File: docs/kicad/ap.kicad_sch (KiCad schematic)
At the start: 5 parts, among them U5 ESP32-DevKitC

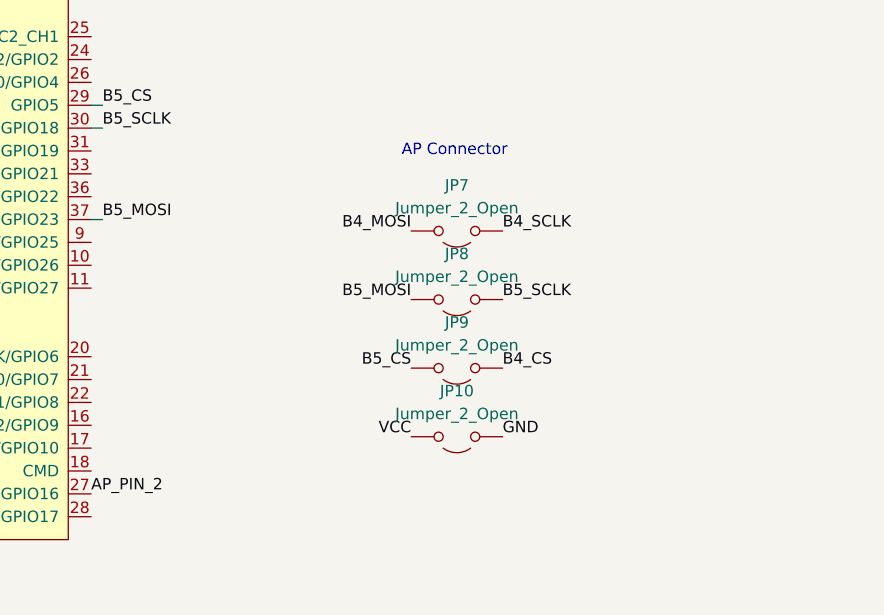
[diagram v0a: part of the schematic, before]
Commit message: Shrink PCB + minor modifications
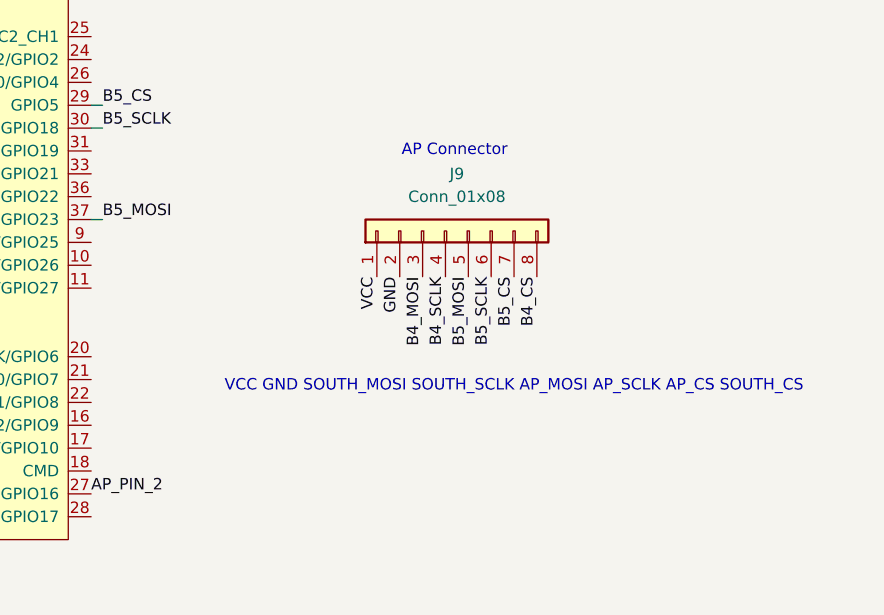
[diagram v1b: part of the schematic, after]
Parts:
- removed JP10, JP7, JP8, JP9: Jumper_2_Open, Connector_PinSocket_1.00mm:PinSocket_1x02_P1.00mm_Vertical, symbol Jumper:Jumper_2_Open
- added J9: Conn_01x08, Connector_PinHeader_1.27mm:PinHeader_1x08_P1.27mm_Vertical, symbol Connector_Generic:Conn_01x08
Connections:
- net B4_CS: now also J9.8 (Pin_8)
- net B4_MOSI: now also J9.3 (Pin_3)
- net B4_SCLK: now also J9.4 (Pin_4)
- net B5_CS: now also J9.7 (Pin_7)
- net B5_MOSI: now also J9.5 (Pin_5)
- net B5_SCLK: now also J9.6 (Pin_6)
- net GND1: now also J9.2 (Pin_2)
- net VCC: now also J9.1 (Pin_1)
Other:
- note added: "VCC GND SOUTH_MOSI SOUTH_SCLK AP_MOSI AP_SCLK AP_CS SOUTH_CS"

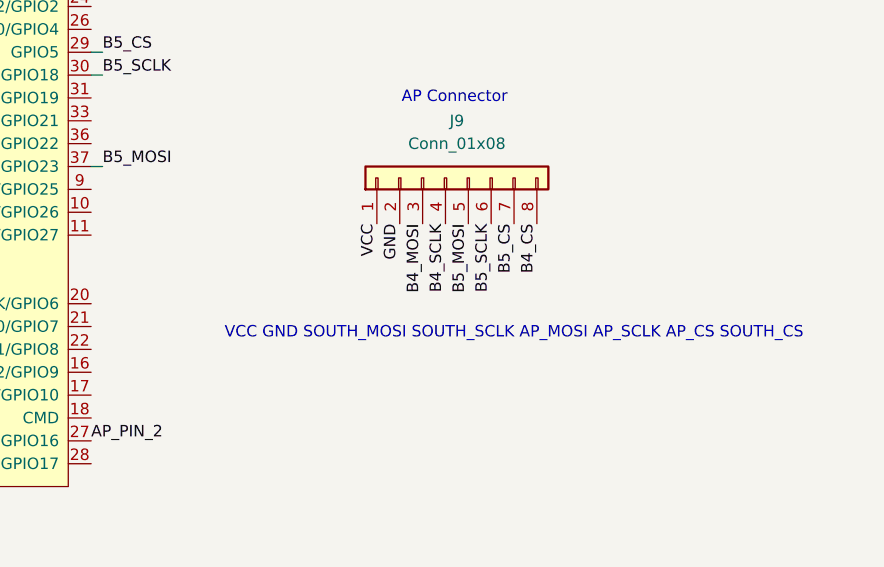
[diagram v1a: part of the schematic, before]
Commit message: used 8mm routes 1mm clearance, having some gnd islands
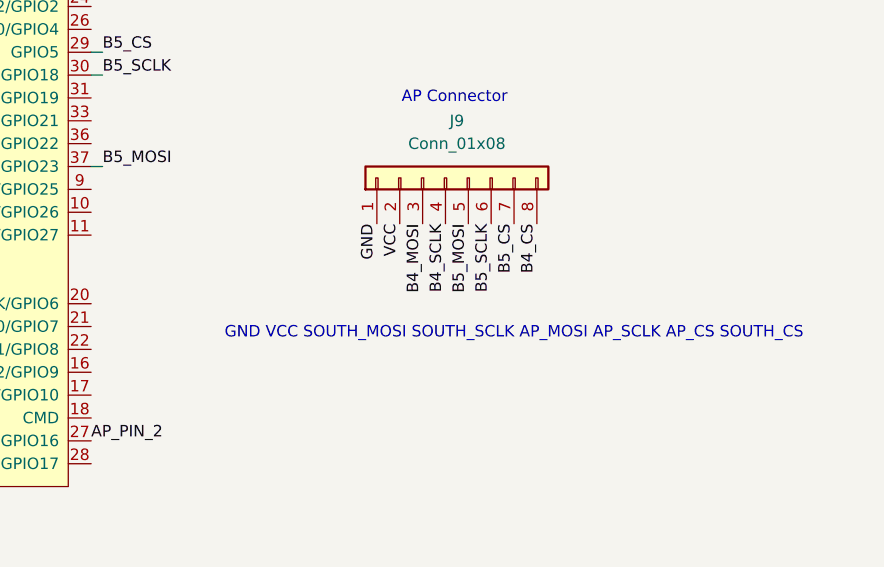
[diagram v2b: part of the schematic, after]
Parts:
- J9: footprint Connector_PinHeader_1.27mm:PinHeader_1x08_P1.27mm_Vertical -> Connector_PinSocket_2.54mm:PinSocket_1x08_P2.54mm_Vertical
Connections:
- net GND1: now also J9.1 (Pin_1); no longer J9.2 (Pin_2)
- net VCC: now also J9.2 (Pin_2); no longer J9.1 (Pin_1)
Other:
- note added: "GND VCC SOUTH_MOSI SOUTH_SCLK AP_MOSI AP_SCLK AP_CS SOUTH_CS"
- note removed: "VCC GND SOUTH_MOSI SOUTH_SCLK AP_MOSI AP_SCLK AP_CS SOUTH_CS"
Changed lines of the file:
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@@
 		)
 	)
-	(text "VCC GND SOUTH_MOSI SOUTH_SCLK AP_MOSI AP_SCLK AP_CS SOUTH_CS"
+	(text "GND VCC SOUTH_MOSI SOUTH_SCLK AP_MOSI AP_SCLK AP_CS SOUTH_CS"
 		(exclude_from_sim no)
 		(at 137.16 80.772 0)
@@
 		)
 	)
-	(label "GND"
-		(at 124.46 68.58 270)
-		(fields_autoplaced yes)
-		(effects
-			(font
-				(size 1.27 1.27)
-			)
-			(justify right bottom)
-		)
-	)
 	(label "B4_SCLK"
 		(at 129.54 68.58 270)
@@
 		)
 	)
+	(label "VCC"
+		(at 124.46 68.58 270)
+		(fields_autoplaced yes)
+		(effects
+			(font
+				(size 1.27 1.27)
+			)
+			(justify right bottom)
+		)
+	)
 	(label "B5_SCLK"
 		(at 134.62 68.58 270)
@@
 		)
 	)
-	(label "VCC"
-		(at 121.92 68.58 270)
-		(fields_autoplaced yes)
-		(effects
-			(font
-				(size 1.27 1.27)
-			)
-			(justify right bottom)
-		)
-	)
 	(label "GND"
 		(at 57.15 100.33 270)
@@
 	(label "B4_SCLK"
 		(at 22.86 52.07 180)
+		(fields_autoplaced yes)
+		(effects
+			(font
+				(size 1.27 1.27)
+			)
+			(justify right bottom)
+		)
+	)
+	(label "GND"
+		(at 121.92 68.58 270)
 		(fields_autoplaced yes)
 		(effects
@@
 			)
 		)
-		(property "Footprint" "Connector_PinHeader_1.27mm:PinHeader_1x08_P1.27mm_Vertical"
+		(property "Footprint" "Connector_PinSocket_2.54mm:PinSocket_1x08_P2.54mm_Vertical"
 			(at 129.54 63.5 0)
 			(effects

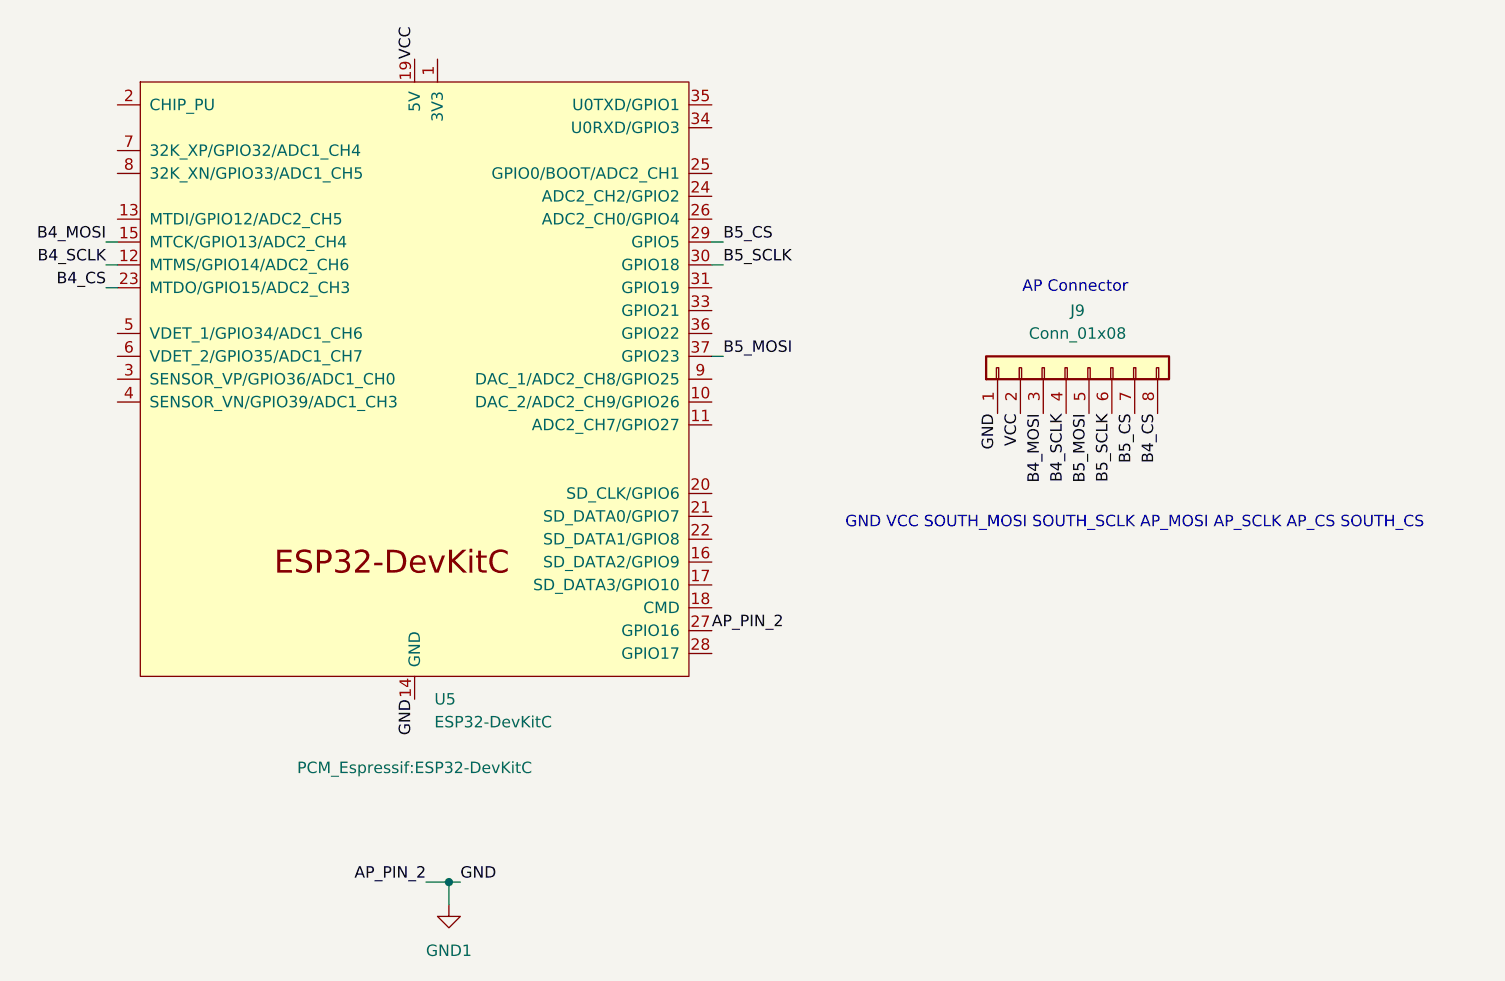
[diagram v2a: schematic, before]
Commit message: use rj45 to connect
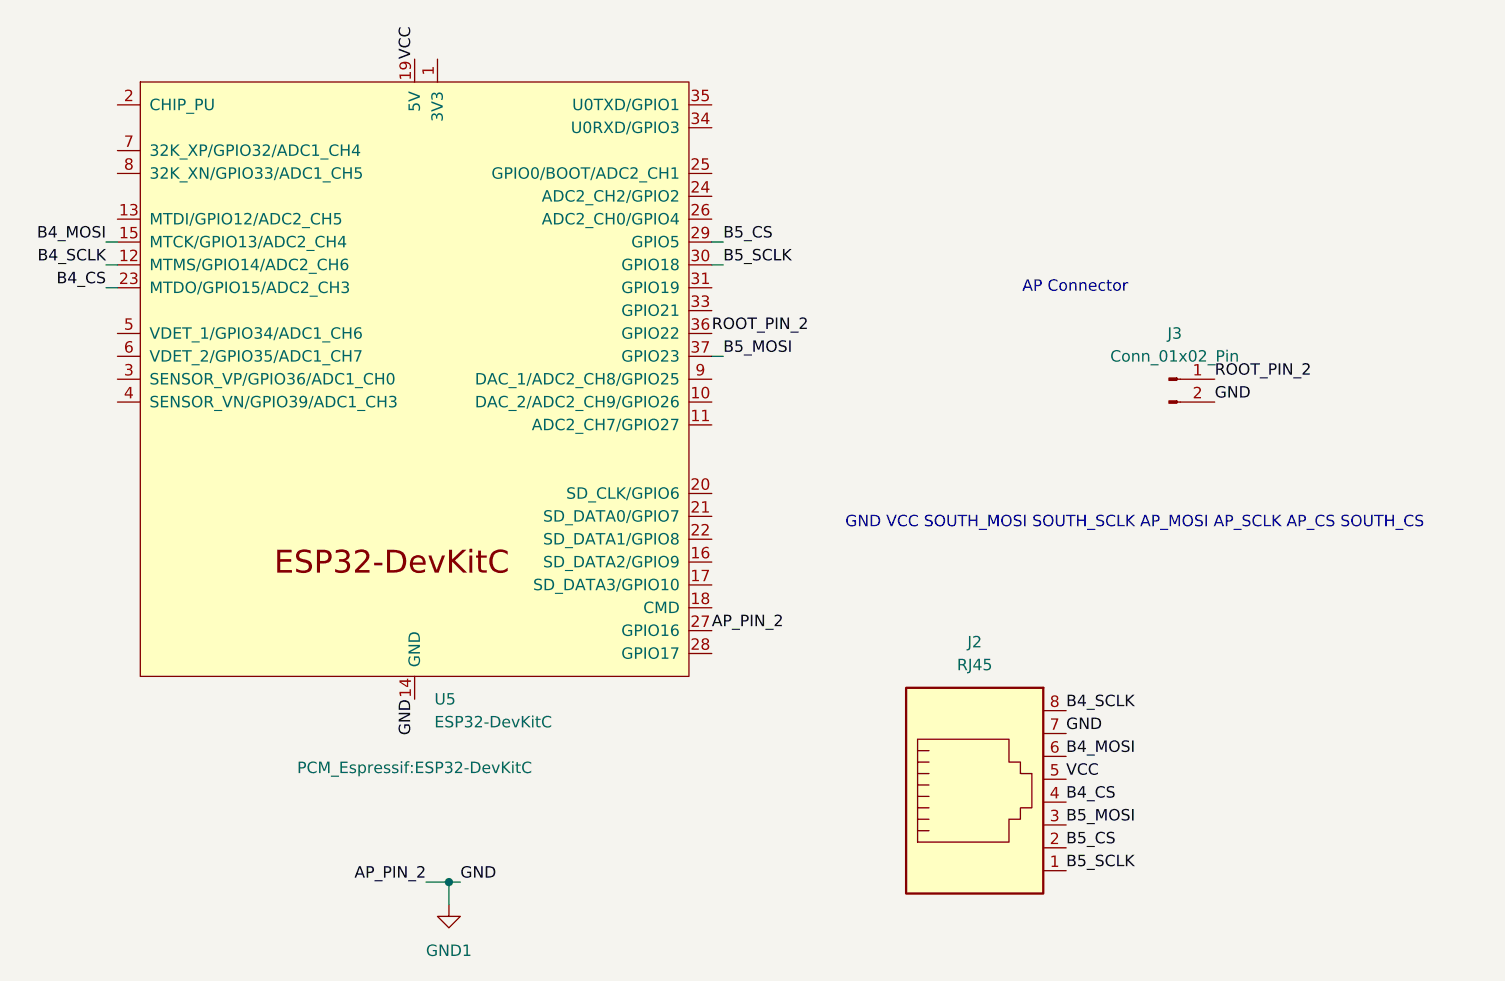
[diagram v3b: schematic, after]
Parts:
- removed J9: Conn_01x08, Connector_PinSocket_2.54mm:PinSocket_1x08_P2.54mm_Vertical, symbol Connector_Generic:Conn_01x08
- added J2: RJ45, Connector_RJ:RJ45_Amphenol_RJMG1BD3B8K1ANR, symbol Connector:RJ45
- added J3: Conn_01x02_Pin, Connector_PinHeader_2.54mm:PinHeader_1x02_P2.54mm_Vertical, symbol Connector:Conn_01x02_Pin
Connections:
- net B4_CS: now also J2.4
- net B4_MOSI: now also J2.6
- net B4_SCLK: now also J2.8
- net B5_CS: now also J2.2
- net B5_MOSI: now also J2.3
- net B5_SCLK: now also J2.1
- net GND1: now also J2.7, J3.2 (Pin_2)
- net VCC: now also J2.5
- net ROOT_PIN_2: now reaches U5.36 (GPIO22)
- net ROOT_PIN_2: now also J3.1 (Pin_1)
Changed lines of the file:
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@@
-		)
-	)
-	(label "B5_CS"
-		(at 137.16 68.58 270)
-		(fields_autoplaced yes)
-		(effects
-			(font
-				(size 1.27 1.27)
-			)
-			(justify right bottom)
-		)
-	)
-	(label "B4_SCLK"
-		(at 129.54 68.58 270)
-		(fields_autoplaced yes)
-		(effects
-			(font
-				(size 1.27 1.27)
-			)
-			(justify right bottom)
 		)
 	)
@@
 		)
 	)
-	(label "VCC"
-		(at 124.46 68.58 270)
-		(fields_autoplaced yes)
-		(effects
-			(font
-				(size 1.27 1.27)
-			)
-			(justify right bottom)
-		)
-	)
-	(label "B5_SCLK"
-		(at 134.62 68.58 270)
-		(fields_autoplaced yes)
-		(effects
-			(font
-				(size 1.27 1.27)
-			)
-			(justify right bottom)
+	(label "GND"
+		(at 146.05 67.31 0)
+		(fields_autoplaced yes)
+		(effects
+			(font
+				(size 1.27 1.27)
+			)
+			(justify left bottom)
+		)
+	)
+	(label "B4_MOSI"
+		(at 129.54 106.68 0)
+		(fields_autoplaced yes)
+		(effects
+			(font
+				(size 1.27 1.27)
+			)
+			(justify left bottom)
+		)
+	)
+	(label "B5_CS"
+		(at 129.54 116.84 0)
+		(fields_autoplaced yes)
+		(effects
+			(font
+				(size 1.27 1.27)
+			)
+			(justify left bottom)
 		)
 	)
@@
 		)
 	)
+	(label "GND"
+		(at 129.54 104.14 0)
+		(fields_autoplaced yes)
+		(effects
+			(font
+				(size 1.27 1.27)
+			)
+			(justify left bottom)
+		)
+	)
 	(label "B5_CS"
 		(at 91.44 49.53 0)
@@
 		)
 	)
-	(label "B5_MOSI"
-		(at 132.08 68.58 270)
-		(fields_autoplaced yes)
-		(effects
-			(font
-				(size 1.27 1.27)
-			)
-			(justify right bottom)
+	(label "ROOT_PIN_2"
+		(at 90.17 59.69 0)
+		(fields_autoplaced yes)
+		(effects
+			(font
+				(size 1.27 1.27)
+			)
+			(justify left bottom)
 		)
 	)
@@
 		)
 	)
-	(label "B4_CS"
-		(at 139.7 68.58 270)
-		(fields_autoplaced yes)
-		(effects
-			(font
-				(size 1.27 1.27)
-			)
-			(justify right bottom)
-		)
-	)
 	(label "B4_SCLK"
 		(at 22.86 52.07 180)
@@
 		)
 	)
-	(label "GND"
-		(at 121.92 68.58 270)
-		(fields_autoplaced yes)
-		(effects
-			(font
-				(size 1.27 1.27)
-			)
-			(justify right bottom)
+	(label "B5_SCLK"
+		(at 129.54 119.38 0)
+		(fields_autoplaced yes)
+		(effects
+			(font
+				(size 1.27 1.27)
+			)
+			(justify left bottom)
+		)
+	)
+	(label "B5_MOSI"
+		(at 129.54 114.3 0)
+		(fields_autoplaced yes)
+		(effects
+			(font
+				(size 1.27 1.27)
+			)
+			(justify left bottom)
+		)
+	)
+	(label "VCC"
+		(at 129.54 109.22 0)
+		(fields_autoplaced yes)
+		(effects
+			(font
+				(size 1.27 1.27)
+			)
+			(justify left bottom)
 		)
 	)
@@
 	)
 	(label "B4_CS"
+		(at 129.54 111.76 0)
+		(fields_autoplaced yes)
+		(effects
+			(font
+				(size 1.27 1.27)
+			)
+			(justify left bottom)
+		)
+	)
+	(label "B4_CS"
 		(at 22.86 54.61 180)
 		(fields_autoplaced yes)
@@
 		)
 	)
-	(label "B4_MOSI"
-		(at 127 68.58 270)
-		(fields_autoplaced yes)
-		(effects
-			(font
-				(size 1.27 1.27)
-			)
-			(justify right bottom)
+	(label "ROOT_PIN_2"
+		(at 146.05 64.77 0)
+		(fields_autoplaced yes)
+		(effects
+			(font
+				(size 1.27 1.27)
+			)
+			(justify left bottom)
+		)
+	)
+	(label "B4_SCLK"
+		(at 129.54 101.6 0)
+		(fields_autoplaced yes)
+		(effects
+			(font
+				(size 1.27 1.27)
+			)
+			(justify left bottom)
 		)
 	)
@@
 	)
 	(symbol
-		(lib_id "Connector_Generic:Conn_01x08")
-		(at 129.54 63.5 90)
+		(lib_id "Connector:Conn_01x02_Pin")
+		(at 140.97 64.77 0)
 		(unit 1)
 		(exclude_from_sim no)
@@
 		(dnp no)
 		(fields_autoplaced yes)
-		(property "Reference" "J9"
-			(at 130.81 57.15 90)
-			(effects
-				(font
-					(size 1.27 1.27)
-				)
-			)
-		)
-		(property "Value" "Conn_01x08"
-			(at 130.81 59.69 90)
-			(effects
-				(font
-					(size 1.27 1.27)
-				)
-			)
-		)
-		(property "Footprint" "Connector_PinSocket_2.54mm:PinSocket_1x08_P2.54mm_Vertical"
-			(at 129.54 63.5 0)
+		(property "Reference" "J3"
+			(at 141.605 59.69 0)
+			(effects
+				(font
+					(size 1.27 1.27)
+				)
+			)
+		)
+		(property "Value" "Conn_01x02_Pin"
+			(at 141.605 62.23 0)
+			(effects
+				(font
+					(size 1.27 1.27)
+				)
+			)
+		)
+		(property "Footprint" "Connector_PinHeader_2.54mm:PinHeader_1x02_P2.54mm_Vertical"
+			(at 140.97 64.77 0)
 			(effects
 				(font
@@
 		)
 		(property "Datasheet" "~"
-			(at 129.54 63.5 0)
-			(effects
-				(font
-					(size 1.27 1.27)
-				)
-				(hide yes)
-			)
-		)
-		(property "Description" "Generic connector, single row, 01x08, script generated (kicad-library-utils/schlib/autogen/connector/)"
-			(at 129.54 63.5 0)
-			(effects
-				(font
-					(size 1.27 1.27)
-				)
-				(hide yes)
-			)
-		)
-		(pin "7"
-		)
-		(pin "8"
-		)
-		(pin "4"
-		)
-		(pin "5"
-		)
-		(pin "6"
-		)
-		(pin "3"
+			(at 140.97 64.77 0)
+			(effects
+				(font
+					(size 1.27 1.27)
+				)
+				(hide yes)
+			)
+		)
+		(property "Description" "Generic connector, single row, 01x02, script generated"
+			(at 140.97 64.77 0)
+			(effects
+				(font
+					(size 1.27 1.27)
+				)
+				(hide yes)
+			)
+		)
+		(pin "2"
 		)
 		(pin "1"
-		)
-		(pin "2"
 		)
 		(instances
 			(project ""
 				(path "/edfda3a5-48f3-494d-b8b7-17b5dc6cb08d/4c067cb0-c7fc-4a9d-897e-f207a21c8bf4"
-					(reference "J9")
+					(reference "J3")
 					(unit 1)
 				)
@@
 					(unit 1)
 				)
+			)
+		)
+	)
+	(symbol
+		(lib_id "Connector:RJ45")
+		(at 119.38 111.76 0)
+		(unit 1)
+		(exclude_from_sim no)
+		(in_bom yes)
+		(on_board yes)
+		(dnp no)
+		(fields_autoplaced yes)
+		(property "Reference" "J2"
+			(at 119.38 93.98 0)
+			(effects
+				(font
+					(size 1.27 1.27)
+				)
+			)
+		)
+		(property "Value" "RJ45"
+			(at 119.38 96.52 0)
+			(effects
+				(font
+					(size 1.27 1.27)
+				)
+			)
+		)
+		(property "Footprint" "Connector_RJ:RJ45_Amphenol_RJMG1BD3B8K1ANR"
+			(at 119.38 111.125 90)
+			(effects
+				(font
+					(size 1.27 1.27)
+				)
+				(hide yes)
+			)
+		)
+		(property "Datasheet" "~"
+			(at 119.38 111.125 90)
+			(effects
+				(font
+					(size 1.27 1.27)
+				)
+				(hide yes)
+			)
+		)
+		(property "Description" "RJ connector, 8P8C (8 positions 8 connected)"
+			(at 119.38 111.76 0)
+			(effects
+				(font
+					(size 1.27 1.27)
+				)
+				(hide yes)
+			)
+		)
+		(pin "7"
+		)
+		(pin "8"
+		)
+		(pin "5"
+		)
+		(pin "6"
+		)
+		(pin "3"
+		)
+		(pin "2"
+		)
+		(pin "4"
+		)
+		(pin "1"
+		)
+		(instances
+			(project "node"
+				(path "/edfda3a5-48f3-494d-b8b7-17b5dc6cb08d/4c067cb0-c7fc-4a9d-897e-f207a21c8bf4"
+					(reference "J2")
+					(unit 1)
+				)
